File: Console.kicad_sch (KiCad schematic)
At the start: 4 parts

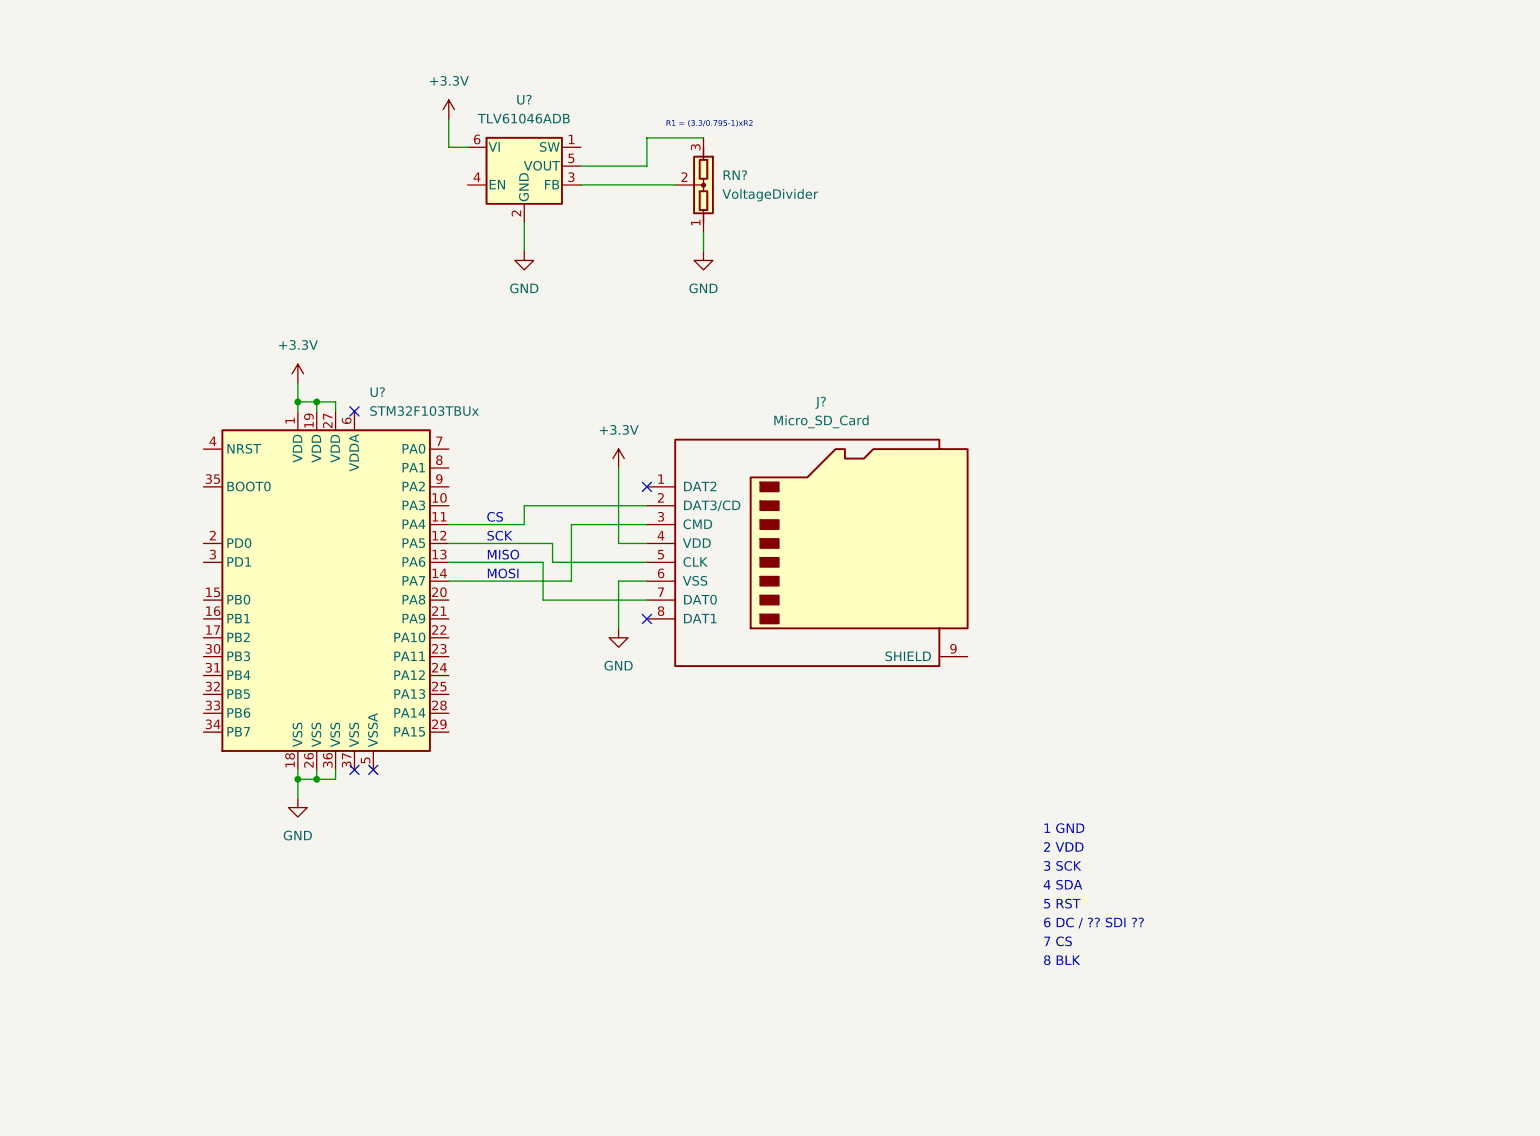
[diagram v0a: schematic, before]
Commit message: small changes to schematics
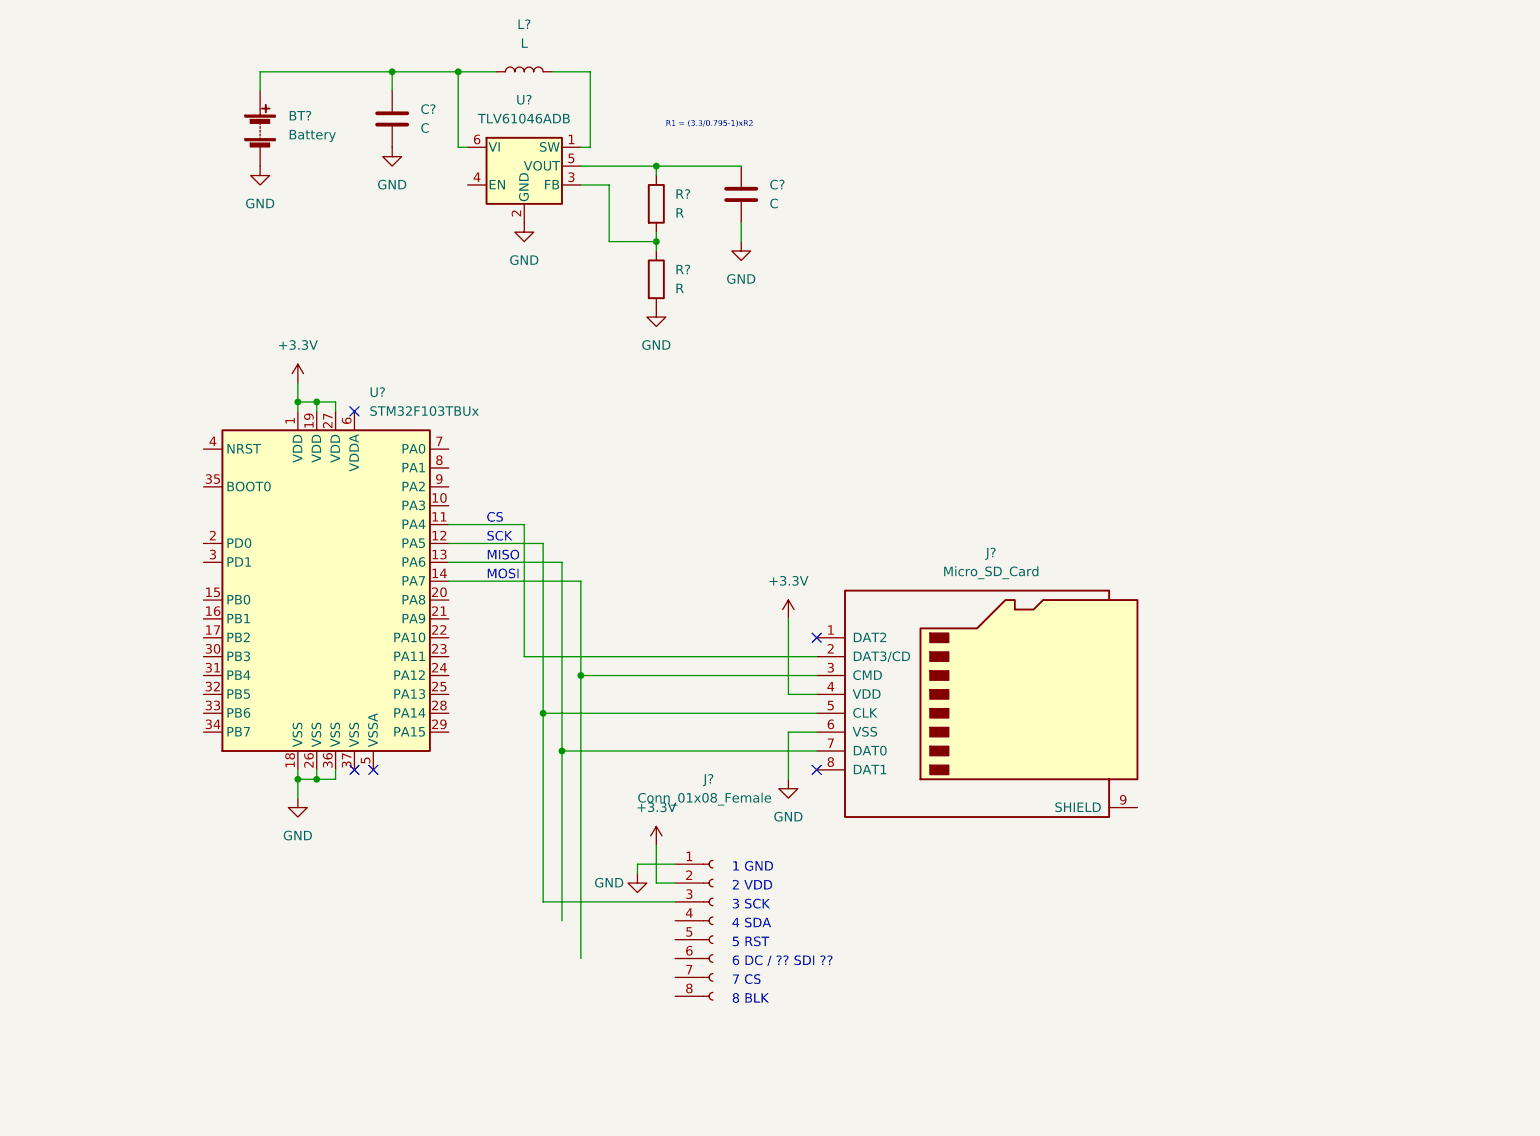
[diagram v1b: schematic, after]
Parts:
- removed RN?: VoltageDivider, symbol Device:VoltageDivider
- added BT?: Battery, symbol Device:Battery
- added C? (x2): C, symbol Device:C
- added J?: Conn_01x08_Female, Connector_PinHeader_2.54mm:PinHeader_1x08_P2.54mm_Vertical, symbol Connector:Conn_01x08_Female
- added L?: L, symbol Device:L
- added R? (x2): R, symbol Device:R
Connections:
- net +3.3V: now also J?.2 (Pin_2); no longer U?.6 (VI)
- net GND: now also BT?.2 (-), C?.2, C?.2, J?.1 (Pin_1), R?.2
- net at J?.5 (CLK), U?.12 (PA5): now also J?.3 (Pin_3)
- net at U?.3 (FB): now also R?.1, R?.2
- net at U?.5 (VOUT): now also C?.1, R?.1
- net at U?.1 (SW): now also L?.2
- new net: BT?.1 (+), C?.1, L?.1, U?.6 (VI)
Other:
- moved on the sheet: J?

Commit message: added buttons to schema and changed routes a bit
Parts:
- removed BT?: Battery, symbol Device:Battery
- added BT?: Battery, symbol Device:Battery
- added C? (x3): C, symbol Device:C
- added D?: D, symbol Device:D
- added F?: Fuse, symbol Device:Fuse
- added Q?: AO3401A, digikey-footprints:SOT-23-3, symbol dk_Transistors-FETs-MOSFETs-Single:AO3401A
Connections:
- net +3.3V: now also C?.1, R?.1, U?.5 (VOUT), C?.1, C?.1, C?.1
- net GND: now also C?.1, L?.1, U?.6 (VI), BT?.2 (-), C?.2, C?.2, C?.2, D?.1 (K)
- net at J?.4 (Pin_4): now also J?.2 (DAT3/CD), U?.11 (PA4)
- net at J?.6 (Pin_6): now also U?.9 (PA2)
- net at J?.7 (Pin_7): now also U?.10 (PA3)
- net GPIO_UP: now reaches U?.20 (PA8)
- net GPIO_LEFT: now reaches U?.21 (PA9)
- net GPIO_DOWN: now reaches U?.22 (PA10)
- net GPIO_RIGHT: now reaches U?.23 (PA11)
- net SWD: now reaches U?.25 (PA13)
- net GPIO_A: now reaches U?.28 (PA14)
- net GPIO_B: now reaches U?.29 (PA15)
- net GPIO_X: now reaches U?.30 (PB3)
- net GPIO_Y: now reaches U?.31 (PB4)
- new net: BT?.1 (+), D?.2 (A)
- no-connect marks 5 -> 7
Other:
- note added: "BULK CAPACITOR???"
- note added: "I2C_SCL"
- note added: "I2C_SDA"
- note added: "T"
- moved on the sheet: C?, J?, L?, R?, U?
